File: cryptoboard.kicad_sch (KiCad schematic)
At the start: 3 parts, among them J1 USB_A, U1 STM32F103C8Tx

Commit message: add resistor
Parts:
- added R1: R_Small, symbol Device:R_Small
- J1: footprint (none) -> Connector_USB:USB_Micro-B_Molex-105017-0001
- KEYBOARD1: renamed from KEYBOARD; footprint (none) -> Connector_USB:USB_A_TE_292303-7_Horizontal
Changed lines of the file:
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@@
   (symbol (lib_id "Connector:USB_A") (at 22.86 69.85 0) (unit 1)
     (in_bom yes) (on_board yes) (dnp no) (fields_autoplaced)
-    (property "Reference" "KEYBOARD" (at 22.86 57.15 0)
+    (property "Reference" "KEYBOARD1" (at 22.86 57.15 0)
       (effects (font (size 1.27 1.27)))
     )
@@
       (effects (font (size 1.27 1.27)))
     )
-    (property "Footprint" "" (at 26.67 71.12 0)
+    (property "Footprint" "Connector_USB:USB_A_TE_292303-7_Horizontal" (at 26.67 71.12 0)
       (effects (font (size 1.27 1.27)) hide)
     )
@@
       (project "cryptoboard"
         (path "/dcd2214c-a8e3-4da9-953a-c4b4305fce7d"
-          (reference "KEYBOARD") (unit 1)
+          (reference "KEYBOARD1") (unit 1)
         )
       )
@@
       (effects (font (size 1.27 1.27)))
     )
-    (property "Footprint" "" (at 26.67 29.21 0)
+    (property "Footprint" "Connector_USB:USB_Micro-B_Molex-105017-0001" (at 26.67 29.21 0)
       (effects (font (size 1.27 1.27)) hide)
     )
@@
         )
       )
+    )
+  )
+  (symbol (lib_id "Device:R_Small") (at 68.58 39.37 0) (unit 1)
+    (in_bom yes) (on_board yes) (dnp no) (fields_autoplaced)
+    (property "Reference" "R1" (at 71.12 38.1 0)
+      (effects (font (size 1.27 1.27)) (justify left))
+    )
+    (property "Value" "R_Small" (at 71.12 40.64 0)
+      (effects (font (size 1.27 1.27)) (justify left))
+    )
+    (property "Footprint" "" (at 68.58 39.37 0)
+      (effects (font (size 1.27 1.27)) hide)
+    )
+    (property "Datasheet" "~" (at 68.58 39.37 0)
+      (effects (font (size 1.27 1.27)) hide)
+    )
+    (pin "1")
+    (pin "2")
+    (instances
+      (project "cryptoboard"
+        (path "/dcd2214c-a8e3-4da9-953a-c4b4305fce7d"
+          (reference "R1") (unit 1)
+        )
+      )

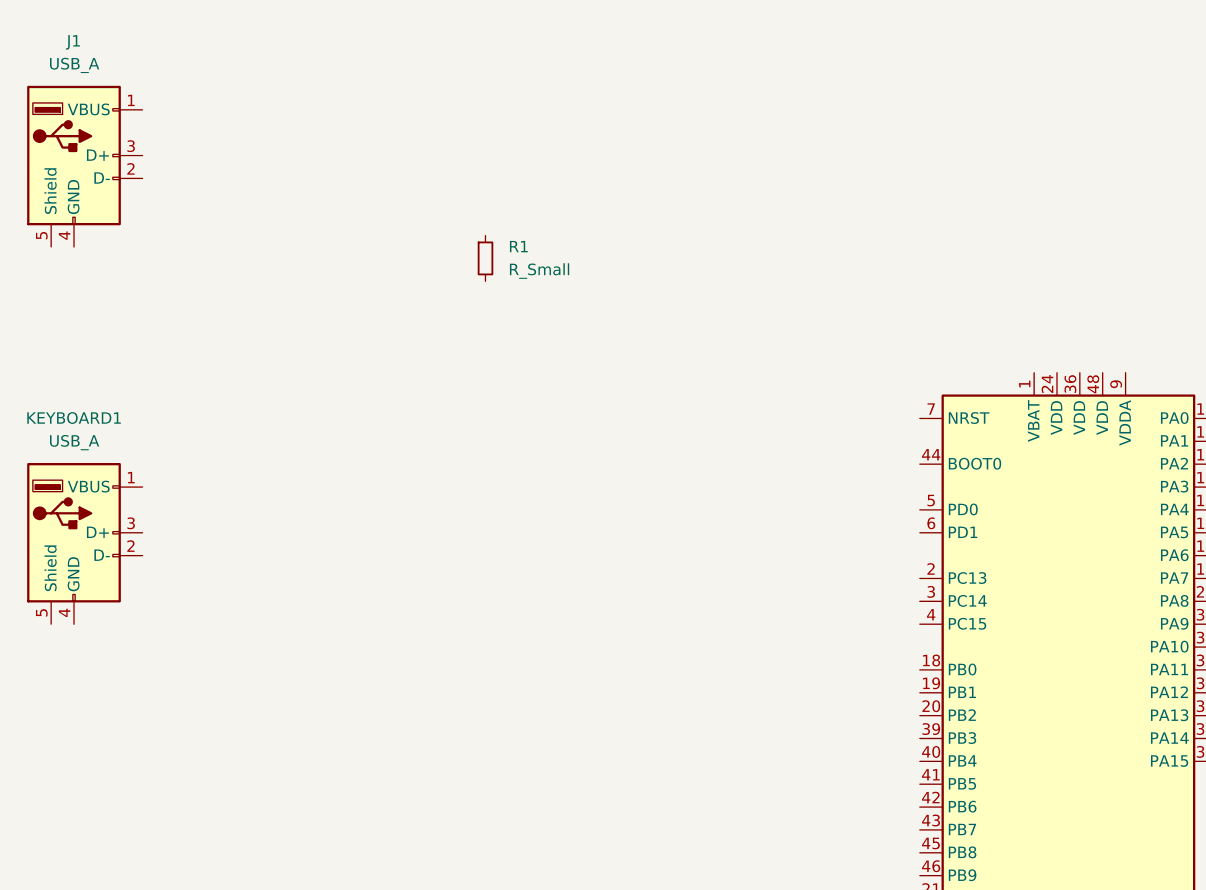
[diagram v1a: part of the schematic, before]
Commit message: add boot connector
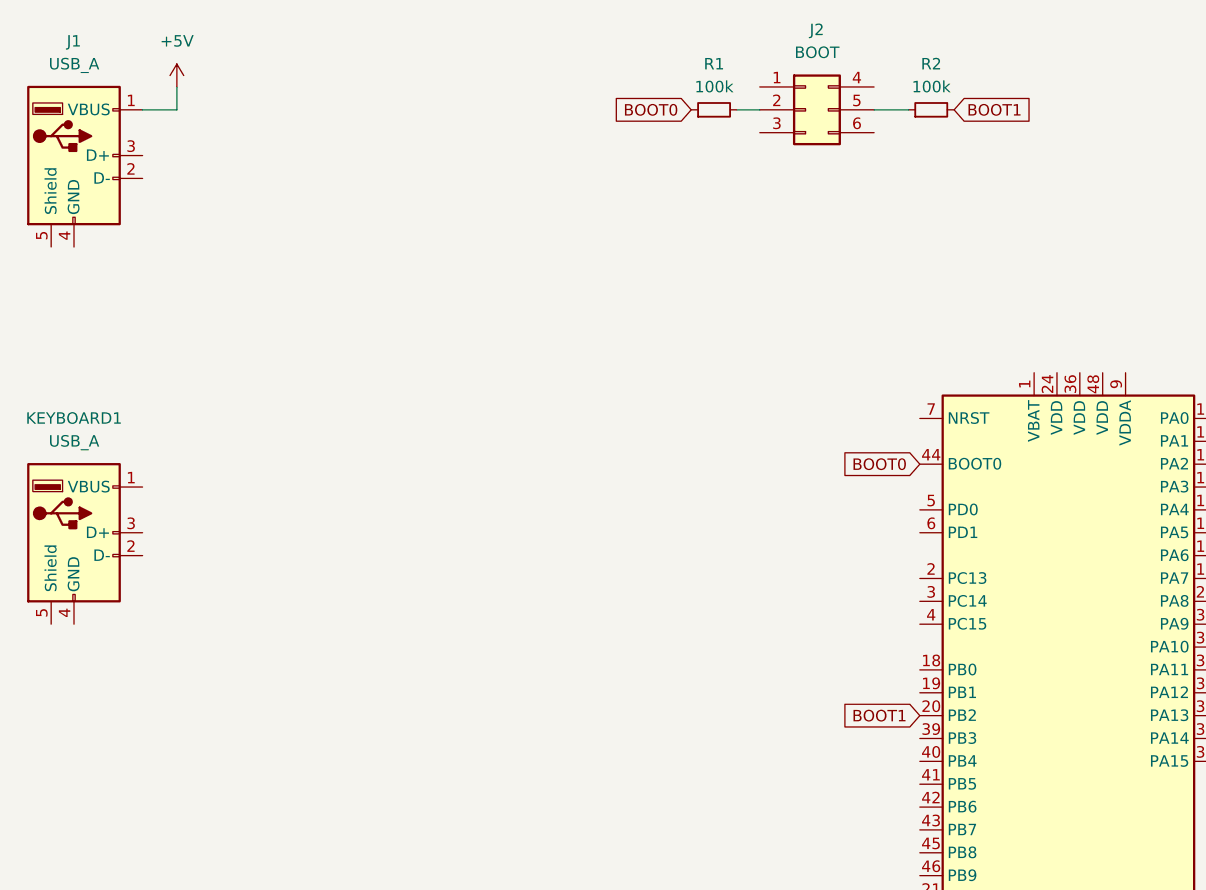
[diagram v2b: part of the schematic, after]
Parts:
- added J2: BOOT, symbol Connector_Generic:Conn_02x03_Top_Bottom
- added R2: 100k, symbol Device:R_Small
- R1: value R_Small -> 100k
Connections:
- net BOOT1: now reaches U1.20 (PB2)
- net BOOT1: now also R2.2
- net BOOT0: now reaches U1.44 (BOOT0)
- net BOOT0: now also R1.1
- net +5V: now reaches J1.1 (VBUS)
- net at R1.2: now also J2.2 (Pin_2)
- new net: J2.5 (Pin_5), R2.1
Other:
- moved on the sheet: R1
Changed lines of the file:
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@@
 (kicad_sch (version 20230121) (generator eeschema)
   (paper "A4")
+  (wire (pts (xy 96.52 22.86) (xy 99.06 22.86))
+    (stroke (width 0) (type default))
+  )
+  (wire (pts (xy 111.76 22.86) (xy 115.57 22.86))
+    (stroke (width 0) (type default))
+  )
+  (wire (pts (xy 34.29 22.86) (xy 34.29 20.32))
+    (stroke (width 0) (type default))
+  )
+  (wire (pts (xy 30.48 22.86) (xy 34.29 22.86))
+    (stroke (width 0) (type default))
+  )
+  (global_label "BOOT1" (shape input) (at 116.84 90.17 180) (fields_autoplaced)
+    (effects (font (size 1.27 1.27)) (justify right))
+    (property "Intersheetrefs" "${INTERSHEET_REFS}" (at 107.8261 90.17 0)
+      (effects (font (size 1.27 1.27)) (justify right) hide)
+    )
+  )
+  (global_label "BOOT0" (shape input) (at 116.84 62.23 180) (fields_autoplaced)
+    (effects (font (size 1.27 1.27)) (justify right))
+    (property "Intersheetrefs" "${INTERSHEET_REFS}" (at 107.8261 62.23 0)
+      (effects (font (size 1.27 1.27)) (justify right) hide)
+    )
+  )
+  (global_label "BOOT1" (shape input) (at 120.65 22.86 0) (fields_autoplaced)
+    (effects (font (size 1.27 1.27)) (justify left))
+    (property "Intersheetrefs" "${INTERSHEET_REFS}" (at 129.6639 22.86 0)
+      (effects (font (size 1.27 1.27)) (justify left) hide)
+    )
+  )
+  (global_label "BOOT0" (shape input) (at 91.44 22.86 180) (fields_autoplaced)
+    (effects (font (size 1.27 1.27)) (justify right))
+    (property "Intersheetrefs" "${INTERSHEET_REFS}" (at 82.4261 22.86 0)
+      (effects (font (size 1.27 1.27)) (justify right) hide)
+    )
+  )
   (symbol (lib_id "MCU_ST_STM32F1:STM32F103C8Tx") (at 132.08 92.71 0) (unit 1)
     (in_bom yes) (on_board yes) (dnp no) (fields_autoplaced)
@@
     )
   )
+  (symbol (lib_id "power:+5V") (at 34.29 20.32 0) (unit 1)
+    (in_bom yes) (on_board yes) (dnp no) (fields_autoplaced)
+    (property "Reference" "#PWR01" (at 34.29 24.13 0)
+      (effects (font (size 1.27 1.27)) hide)
+    )
+    (property "Value" "+5V" (at 34.29 15.24 0)
+      (effects (font (size 1.27 1.27)))
+    )
+    (property "Footprint" "" (at 34.29 20.32 0)
+      (effects (font (size 1.27 1.27)) hide)
+    )
+    (property "Datasheet" "" (at 34.29 20.32 0)
+      (effects (font (size 1.27 1.27)) hide)
+    )
+    (pin "1")
+    (instances
+      (project "cryptoboard"
+        (path "/dcd2214c-a8e3-4da9-953a-c4b4305fce7d"
+          (reference "#PWR01") (unit 1)
+        )
+      )
+    )
+  )
   (symbol (lib_id "Connector:USB_A") (at 22.86 69.85 0) (unit 1)
     (in_bom yes) (on_board yes) (dnp no) (fields_autoplaced)
@@
     )
   )
-  (symbol (lib_id "Device:R_Small") (at 68.58 39.37 0) (unit 1)
-    (in_bom yes) (on_board yes) (dnp no) (fields_autoplaced)
-    (property "Reference" "R1" (at 71.12 38.1 0)
-      (effects (font (size 1.27 1.27)) (justify left))
-    )
-    (property "Value" "R_Small" (at 71.12 40.64 0)
-      (effects (font (size 1.27 1.27)) (justify left))
-    )
-    (property "Footprint" "" (at 68.58 39.37 0)
-      (effects (font (size 1.27 1.27)) hide)
-    )
-    (property "Datasheet" "~" (at 68.58 39.37 0)
-      (effects (font (size 1.27 1.27)) hide)
-    )
+  (symbol (lib_id "Device:R_Small") (at 118.11 22.86 90) (unit 1)
+    (in_bom yes) (on_board yes) (dnp no) (fields_autoplaced)
+    (property "Reference" "R2" (at 118.11 17.78 90)
+      (effects (font (size 1.27 1.27)))
+    )
+    (property "Value" "100k" (at 118.11 20.32 90)
+      (effects (font (size 1.27 1.27)))
+    )
+    (property "Footprint" "" (at 118.11 22.86 0)
+      (effects (font (size 1.27 1.27)) hide)
+    )
+    (property "Datasheet" "~" (at 118.11 22.86 0)
+      (effects (font (size 1.27 1.27)) hide)
+    )
+    (pin "1")
+    (pin "2")
+    (instances
+      (project "cryptoboard"
+        (path "/dcd2214c-a8e3-4da9-953a-c4b4305fce7d"
+          (reference "R2") (unit 1)
+        )
+      )
+    )
+  )
+  (symbol (lib_id "Connector_Generic:Conn_02x03_Top_Bottom") (at 104.14 22.86 0) (unit 1)
+    (in_bom yes) (on_board yes) (dnp no) (fields_autoplaced)
+    (property "Reference" "J2" (at 105.41 13.97 0)
+      (effects (font (size 1.27 1.27)))
+    )
+    (property "Value" "BOOT" (at 105.41 16.51 0)
+      (effects (font (size 1.27 1.27)))
+    )
+    (property "Footprint" "" (at 104.14 22.86 0)
+      (effects (font (size 1.27 1.27)) hide)
+    )
+    (property "Datasheet" "~" (at 104.14 22.86 0)
+      (effects (font (size 1.27 1.27)) hide)
+    )
+    (pin "1")
+    (pin "2")
+    (pin "3")
+    (pin "4")
+    (pin "5")
+    (pin "6")
+    (instances
+      (project "cryptoboard"
+        (path "/dcd2214c-a8e3-4da9-953a-c4b4305fce7d"
+          (reference "J2") (unit 1)
+        )
+      )
+    )
+  )
+  (symbol (lib_id "Device:R_Small") (at 93.98 22.86 90) (unit 1)
+    (in_bom yes) (on_board yes) (dnp no) (fields_autoplaced)
+    (property "Reference" "R1" (at 93.98 17.78 90)
+      (effects (font (size 1.27 1.27)))
+    )
+    (property "Value" "100k" (at 93.98 20.32 90)
+      (effects (font (size 1.27 1.27)))
+    )
+    (property "Footprint" "" (at 93.98 22.86 0)
+      (effects (font (size 1.27 1.27)) hide)
+    )
+    (property "Datasheet" "~" (at 93.98 22.86 0)
+      (effects (font (size 1.27 1.27)) hide)
+    )

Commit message: add DC DC
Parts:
- added C1, C2, C3: C_Small, symbol Device:C_Small
- added U2: LM317_SOT-223-3.3V, Package_TO_SOT_SMD:SOT-223-3_TabPin2, symbol Regulator_Linear:LM317_SOT-223
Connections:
- net +5V: now also KEYBOARD1.1 (VBUS), C1.1, U2.3 (VI)
- net GND: now reaches KEYBOARD1.4 (GND)
- net GND: now also J1.4 (GND), C1.2, C2.2, C3.2, U2.1 (ADJ)
- new net +3.3V: C2.1, C3.1, U2.2 (VO)
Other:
- moved on the sheet: J2, R1, R2

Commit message: UPDATE shcema
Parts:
- added R3, R4: 22, Resistor_SMD:R_0603_1608Metric, symbol Device:R_Small
- C1, C2, C3: footprint (none) -> Capacitor_SMD:C_0603_1608Metric
- J2: footprint (none) -> Connector_PinHeader_2.54mm:PinHeader_2x03_P2.54mm_Vertical
- R1, R2: footprint (none) -> Resistor_SMD:R_0603_1608Metric
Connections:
- net PA11: now reaches U1.32 (PA11)
- net PA11: now also R4.2
- net PA12: now reaches U1.33 (PA12)
- net PA12: now also R3.2
- net at KEYBOARD1.2 (D-): now also R4.1
- net at KEYBOARD1.3 (D+): now also R3.1
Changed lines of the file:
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@@
+    (stroke (width 0) (type default))
+  )
+  (wire (pts (xy 40.64 72.39) (xy 39.37 72.39))
     (stroke (width 0) (type default))
   )
@@
     (stroke (width 0) (type default))
   )
+  (wire (pts (xy 40.64 69.85) (xy 39.37 69.85))
+    (stroke (width 0) (type default))
+  )
   (wire (pts (xy 71.12 25.4) (xy 64.77 25.4))
     (stroke (width 0) (type default))
@@
     (stroke (width 0) (type default))
   )
+  (wire (pts (xy 30.48 69.85) (xy 34.29 69.85))
+    (stroke (width 0) (type default))
+  )
   (wire (pts (xy 95.25 25.4) (xy 93.98 25.4))
     (stroke (width 0) (type default))
@@
   (wire (pts (xy 34.29 64.77) (xy 34.29 62.23))
     (stroke (width 0) (type default))
+  )
+  (wire (pts (xy 30.48 72.39) (xy 34.29 72.39))
+    (stroke (width 0) (type default))
+  )
+  (global_label "PA12" (shape input) (at 40.64 69.85 0) (fields_autoplaced)
+    (effects (font (size 1.27 1.27)) (justify left))
+    (property "Intersheetrefs" "${INTERSHEET_REFS}" (at 48.3234 69.85 0)
+      (effects (font (size 1.27 1.27)) (justify left) hide)
+    )
   )
   (global_label "BOOT1" (shape input) (at 116.84 90.17 180) (fields_autoplaced)
@@
     )
   )
+  (global_label "PA11" (shape input) (at 149.86 85.09 0) (fields_autoplaced)
+    (effects (font (size 1.27 1.27)) (justify left))
+    (property "Intersheetrefs" "${INTERSHEET_REFS}" (at 157.5434 85.09 0)
+      (effects (font (size 1.27 1.27)) (justify left) hide)
+    )
+  )
   (global_label "BOOT1" (shape input) (at 154.94 33.02 0) (fields_autoplaced)
     (effects (font (size 1.27 1.27)) (justify left))
@@
     (property "Intersheetrefs" "${INTERSHEET_REFS}" (at 116.7161 33.02 0)
       (effects (font (size 1.27 1.27)) (justify right) hide)
+    )
+  )
+  (global_label "PA12" (shape input) (at 149.86 87.63 0) (fields_autoplaced)
+    (effects (font (size 1.27 1.27)) (justify left))
+    (property "Intersheetrefs" "${INTERSHEET_REFS}" (at 157.5434 87.63 0)
+      (effects (font (size 1.27 1.27)) (justify left) hide)
+    )
+  )
+  (global_label "PA11" (shape input) (at 40.64 72.39 0) (fields_autoplaced)
+    (effects (font (size 1.27 1.27)) (justify left))
+    (property "Intersheetrefs" "${INTERSHEET_REFS}" (at 48.3234 72.39 0)
+      (effects (font (size 1.27 1.27)) (justify left) hide)
     )
   )
@@
       (effects (font (size 1.27 1.27)) (justify left))
     )
-    (property "Footprint" "" (at 64.77 30.48 0)
+    (property "Footprint" "Capacitor_SMD:C_0603_1608Metric" (at 64.77 30.48 0)
       (effects (font (size 1.27 1.27)) hide)
     )
@@
       (effects (font (size 1.27 1.27)) (justify left))
     )
-    (property "Footprint" "" (at 93.98 30.48 0)
+    (property "Footprint" "Capacitor_SMD:C_0603_1608Metric" (at 93.98 30.48 0)
       (effects (font (size 1.27 1.27)) hide)
     )
@@
       (effects (font (size 1.27 1.27)))
     )
-    (property "Footprint" "" (at 152.4 33.02 0)
+    (property "Footprint" "Resistor_SMD:R_0603_1608Metric" (at 152.4 33.02 0)
       (effects (font (size 1.27 1.27)) hide)
     )
@@
         (path "/dcd2214c-a8e3-4da9-953a-c4b4305fce7d"
           (reference "#PWR02") (unit 1)
+        )
+      )
+    )
+  )
+  (symbol (lib_id "Device:R_Small") (at 36.83 72.39 90) (unit 1)
+    (in_bom yes) (on_board yes) (dnp no)
+    (property "Reference" "R4" (at 36.83 77.47 90)
+      (effects (font (size 1.27 1.27)))
+    )
+    (property "Value" "22" (at 36.83 74.93 90)
+      (effects (font (size 1.27 1.27)))
+    )
+    (property "Footprint" "Resistor_SMD:R_0603_1608Metric" (at 36.83 72.39 0)
+      (effects (font (size 1.27 1.27)) hide)
+    )
+    (property "Datasheet" "~" (at 36.83 72.39 0)
+      (effects (font (size 1.27 1.27)) hide)
+    )
+    (pin "1")
+    (pin "2")
+    (instances
+      (project "cryptoboard"
+        (path "/dcd2214c-a8e3-4da9-953a-c4b4305fce7d"
+          (reference "R4") (unit 1)
         )
       )
@@
       (effects (font (size 1.27 1.27)) (justify left))
     )
-    (property "Footprint" "" (at 87.63 30.48 0)
+    (property "Footprint" "Capacitor_SMD:C_0603_1608Metric" (at 87.63 30.48 0)
       (effects (font (size 1.27 1.27)) hide)
     )
@@
       (effects (font (size 1.27 1.27)))
     )
-    (property "Footprint" "" (at 138.43 33.02 0)
+    (property "Footprint" "Connector_PinHeader_2.54mm:PinHeader_2x03_P2.54mm_Vertical" (at 138.43 33.02 0)
       (effects (font (size 1.27 1.27)) hide)
     )
@@
     )
   )
+  (symbol (lib_id "Device:R_Small") (at 36.83 69.85 90) (unit 1)
+    (in_bom yes) (on_board yes) (dnp no) (fields_autoplaced)
+    (property "Reference" "R3" (at 36.83 64.77 90)
+      (effects (font (size 1.27 1.27)))
+    )
+    (property "Value" "22" (at 36.83 67.31 90)
+      (effects (font (size 1.27 1.27)))
+    )
+    (property "Footprint" "Resistor_SMD:R_0603_1608Metric" (at 36.83 69.85 0)
+      (effects (font (size 1.27 1.27)) hide)
+    )
+    (property "Datasheet" "~" (at 36.83 69.85 0)
+      (effects (font (size 1.27 1.27)) hide)
+    )
+    (pin "1")
+    (pin "2")
+    (instances
+      (project "cryptoboard"
+        (path "/dcd2214c-a8e3-4da9-953a-c4b4305fce7d"
+          (reference "R3") (unit 1)
+        )
+      )
+    )
+  )
   (symbol (lib_id "Device:R_Small") (at 128.27 33.02 90) (unit 1)
     (in_bom yes) (on_board yes) (dnp no) (fields_autoplaced)
@@
       (effects (font (size 1.27 1.27)))
     )
-    (property "Footprint" "" (at 128.27 33.02 0)
-      (effects (font (size 1.27 1.27)) hide)
-    )
+    (property "Footprint" "Resistor_SMD:R_0603_1608Metric" (at 128.27 33.02 0)
+      (effects (font (size 1.27 1.27)) hide)
+    )
